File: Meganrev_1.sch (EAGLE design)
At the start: 3 parts

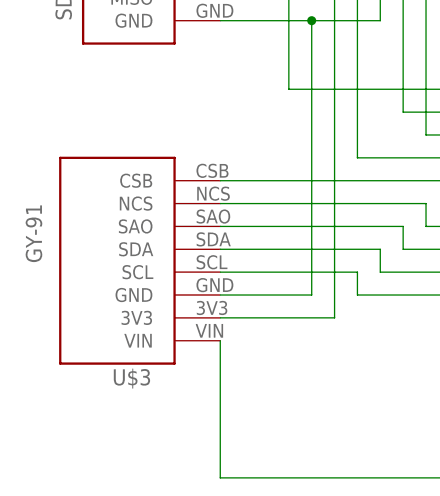
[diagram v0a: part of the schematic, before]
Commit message: update GY-91 nameing to 10DOF-GY-91
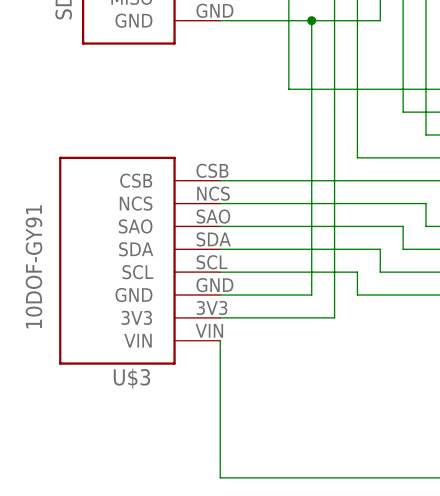
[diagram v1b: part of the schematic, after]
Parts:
- U$3: value GY-91 -> 10DOF-GY91; device macrocketry_2019:GY-91 -> macrocketry_2019:10DOF-GY91
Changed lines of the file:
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@@
 <part name="U$1" library="Teensy_3_and_LC_Series_Boards_v1.4" deviceset="TEENSY_LC_DIL" device=""/>
 <part name="U$2" library="macrocketry_2019" deviceset="SD_CARD_READER" device=""/>
-<part name="U$3" library="macrocketry_2019" deviceset="GY-91" device=""/>
+<part name="U$3" library="macrocketry_2019" deviceset="10DOF-GY91" device=""/>
 </parts>
 <sheets>
